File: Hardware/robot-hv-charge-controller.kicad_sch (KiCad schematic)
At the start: 13 parts, among them J10 OUT 2, J12 OUT 3, J13 RS485, J2 UART, J3 RS485, J4 SW_1, J5 XT60PW-M, J6 XT60PW-M, J7 XT60PW-M, J8 SW_2, J9 OUT 1

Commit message: feat: update footprint power supply
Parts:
- J5, J6, J7: PACKAGE (none) -> Package; Package Package -> (none)

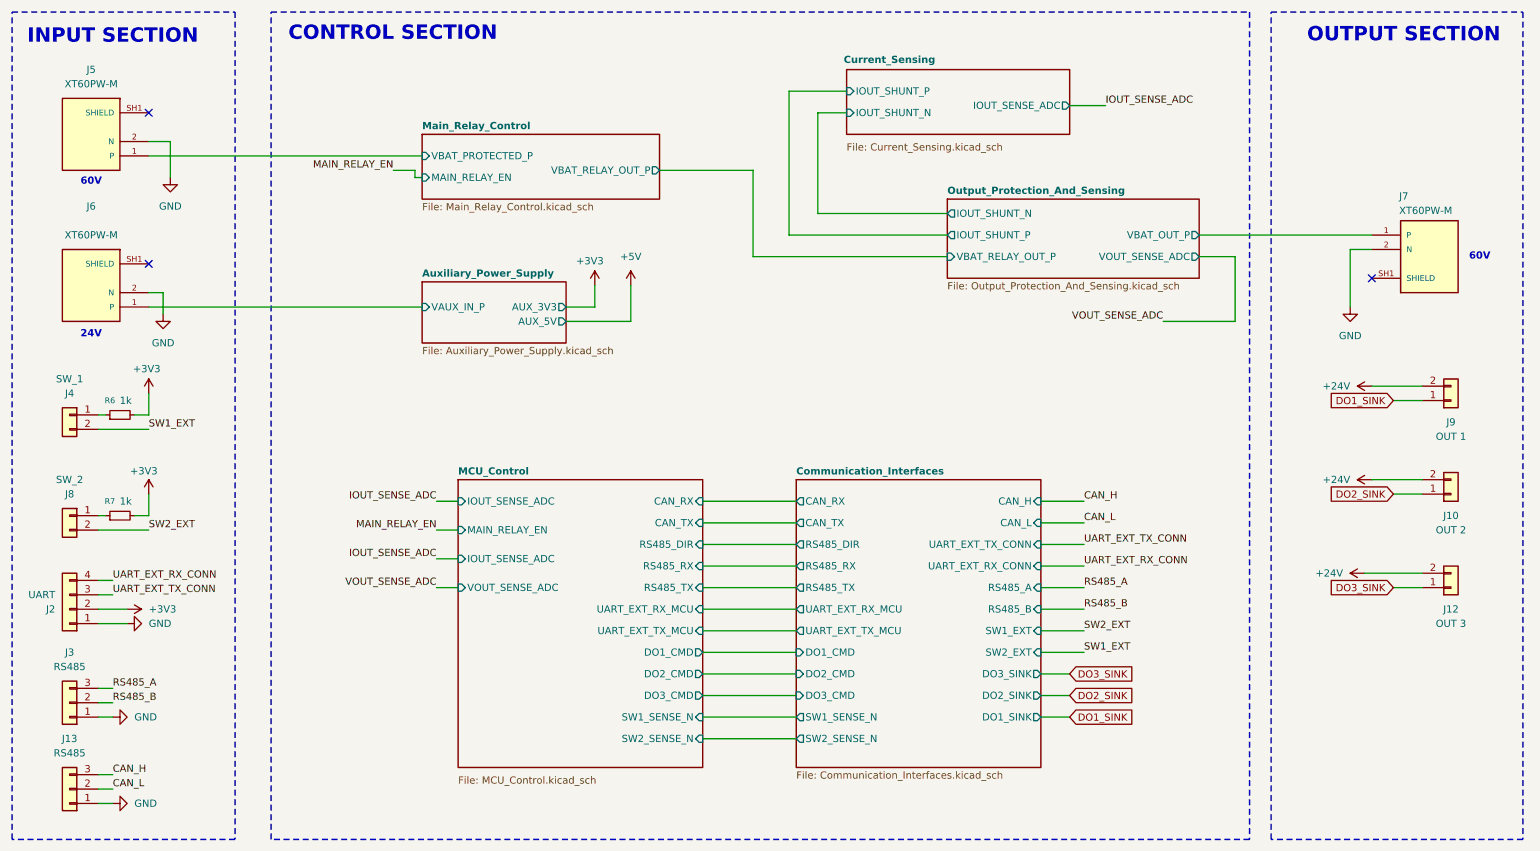
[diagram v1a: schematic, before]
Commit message: feat: update schematic with new components for communication interfaces and export BOM list
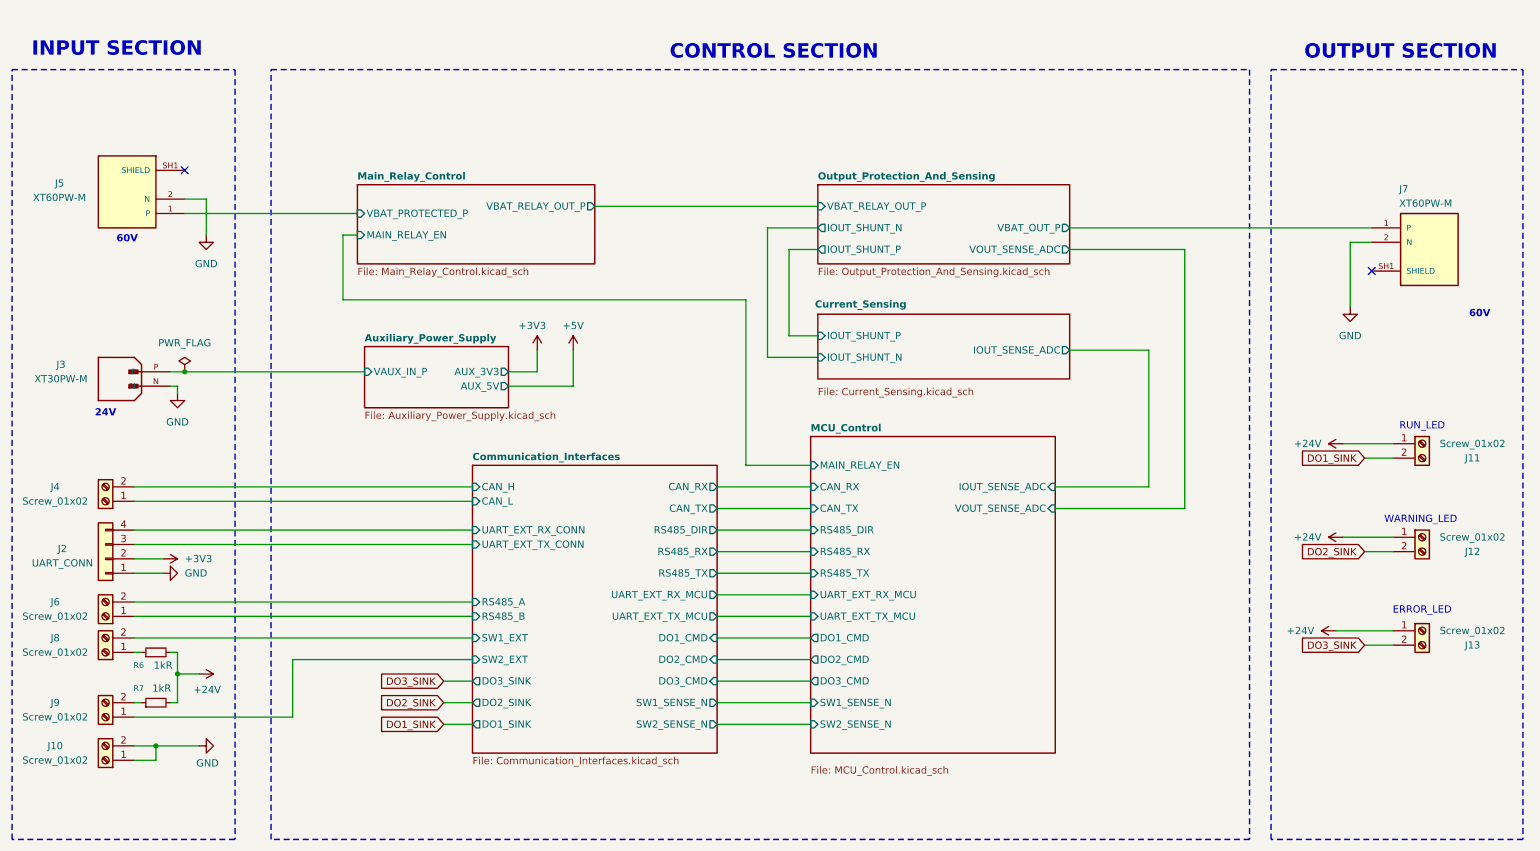
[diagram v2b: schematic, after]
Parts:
- removed J10: OUT 2, symbol Connector_Generic:Conn_01x02
- removed J12: OUT 3, symbol Connector_Generic:Conn_01x02
- removed J13, J3: RS485, symbol Connector_Generic:Conn_01x03
- removed J4: SW_1, symbol Connector_Generic:Conn_01x02
- removed J6: XT60PW-M, XT60PW-M:AMASS_XT60PW-M, symbol XT60PW-M:XT60PW-M
- removed J8: SW_2, symbol Connector_Generic:Conn_01x02
- removed J9: OUT 1, symbol Connector_Generic:Conn_01x02
- added J10, J11, J12, J13, J4, J6, J8, J9: Screw_01x02, TerminalBlock_Phoenix:TerminalBlock_Phoenix_MKDS-1,5-2_1x02_P5.00mm_Horizontal, symbol Connector:Screw_Terminal_01x02
- added J3: XT30PW-M, XT30PW-M:AMASS_XT30PW-M, symbol XT30PW-M:XT30PW-M
- J2: value UART -> UART_CONN; footprint (none) -> Connector_PinHeader_2.54mm:PinHeader_1x04_P2.54mm_Horizontal; Link to Buy (none) -> https://linhkien.cxtvn.com/3053-header-duc-xh254-chan-cong.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; MPN (none) -> XH2.54-4P (bent pin)
- J5, J7: Link to Buy (none) -> https://dientutuyetnga.com/products/xt60pw-m-dau-jack-noi-d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; MANUFACTURER AMASS -> (none); MPN (none) -> XT60PW-M (Amass); Manufacturer (none) -> AMASS
- R6, R7: value 1k -> 1kR; footprint (none) -> Resistor_SMD:R_0805_2012Metric; Link to Buy (none) -> https://linhkien.cxtvn.com/6337-dien-tro-0805-1-thong-so-tu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; MPN (none) -> 1k 0402 1%
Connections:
- net +24V: now also R6.2, R7.2, J11.1 (Pin_1), J12.1 (Pin_1), J13.1 (Pin_1)
- net +3V3: no longer R6.2, R7.2
- net Auxiliary_Power_Supply/VAUX_IN_P: now also J3.P
- net DO1_SINK: now also J11.2 (Pin_2)
- net DO2_SINK: now also J12.2 (Pin_2)
- net DO3_SINK: now also J13.2 (Pin_2)
- net GND: now also J10.1 (Pin_1), J10.2 (Pin_2), J3.N
- net at R6.1: now also J8.1 (Pin_1)
- net at R7.1: now also J9.2 (Pin_2)
- net UART_EXT_RX_CONN renamed Communication_Interfaces/UART_EXT_RX_CONN
- net UART_EXT_TX_CONN renamed Communication_Interfaces/UART_EXT_TX_CONN
- new net Communication_Interfaces/CAN_H: J4.2 (Pin_2)
- new net Communication_Interfaces/CAN_L: J4.1 (Pin_1)
- new net Communication_Interfaces/RS485_A: J6.2 (Pin_2)
- new net Communication_Interfaces/RS485_B: J6.1 (Pin_1)
- new net Communication_Interfaces/SW1_EXT: J8.2 (Pin_2)
- new net Communication_Interfaces/SW2_EXT: J9.1 (Pin_1)
- no-connect marks 3 -> 2
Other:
- note added: "ERROR_LED"
- note added: "RUN_LED"
- note added: "WARNING_LED"
- moved on the sheet: J2, J5, J7, R7

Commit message: Refactor code structure for improved readability and maintainability
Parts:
- J9: value Screw_01x02 -> 01x02
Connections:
- net Main_Relay_Control/VBAT_PROTECTED_P is gone; now on net GND: J5.1 (P)
- net GND: no longer J5.2 (N), J7.2 (N)
- new net 60V_GND: J5.2 (N), J7.2 (N)
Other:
- note added: "24V INPUT"
- note added: "60V INPUT"
- note added: "60V OUTPUT"
- note added: "CAN"
- note added: "GND"
- note added: "RS485"
- note added: "SW1"
- note added: "SW2"
- note added: "UART"
- note removed: "24V"
- note removed: "60V"
- moved on the sheet: J11, J12, J13, J2, J3, J4, J6, J7, J8, J9, R6, R7
